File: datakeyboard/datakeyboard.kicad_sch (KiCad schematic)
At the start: 48 parts, among them Q1 NX2301P, Q2 NX2301P, Q3 NX2301P, Q4 NX2301P, Q5 NX2301P, SW1 SW_Push, SW2 SW_Push, SW3 SW_Push, SW4 SW_Push, SW5 SW_Push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

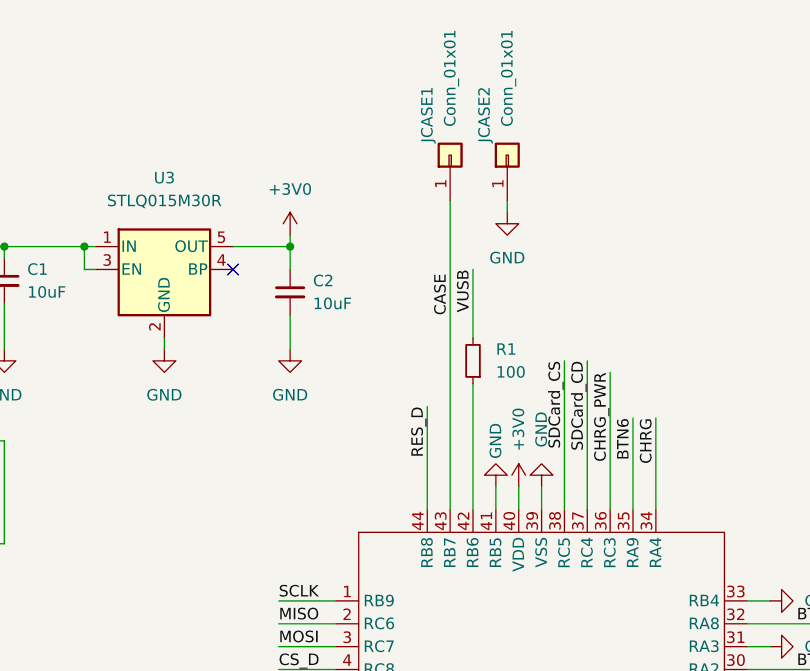
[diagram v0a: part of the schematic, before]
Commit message: Reduce current to increase battery life
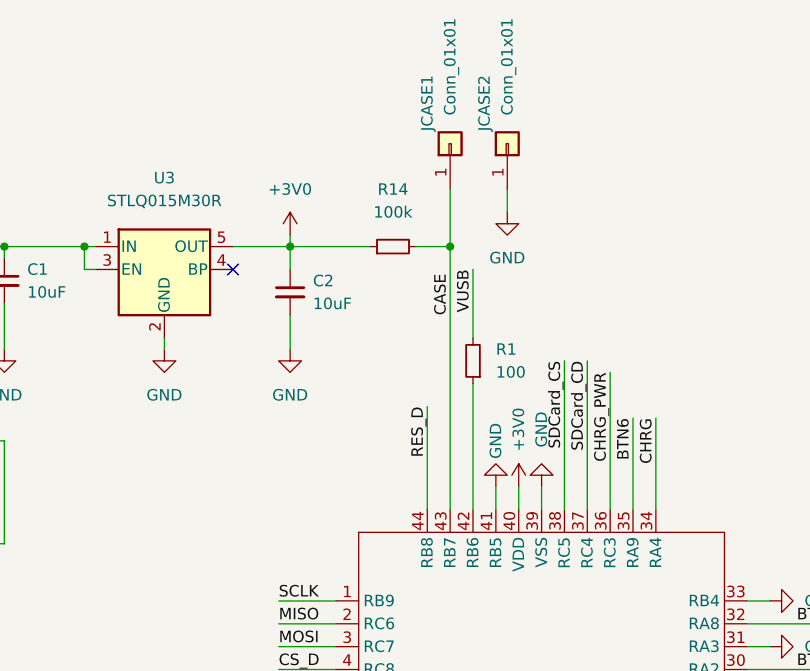
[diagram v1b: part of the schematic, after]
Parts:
- added R14: 100k, Resistor_SMD:R_0805_2012Metric_Pad1.20x1.40mm_HandSolder, symbol Device:R_Small
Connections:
- net +3V0: now also R14.1
- net CASE: now also R14.2
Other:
- moved on the sheet: JCASE1, JCASE2
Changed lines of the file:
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@@
   (junction (at 222.25 107.95) (diameter 0) (color 0 0 0 0)
+  )
+  (junction (at 144.78 38.1) (diameter 0) (color 0 0 0 0)
   )
   (junction (at 48.26 80.01) (diameter 0) (color 0 0 0 0)
@@
     (stroke (width 0) (type default) (color 0 0 0 0))
   )
+  (wire (pts (xy 140.97 38.1) (xy 144.78 38.1))
+    (stroke (width 0) (type default) (color 0 0 0 0))
+  )
   (wire (pts (xy 217.17 53.34) (xy 227.33 53.34))
     (stroke (width 0) (type default) (color 0 0 0 0))
@@
     (stroke (width 0) (type default) (color 0 0 0 0))
   )
+  (wire (pts (xy 127 38.1) (xy 135.89 38.1))
+    (stroke (width 0) (type default) (color 0 0 0 0))
+  )
   (wire (pts (xy 248.92 154.94) (xy 252.73 154.94))
     (stroke (width 0) (type default) (color 0 0 0 0))
@@
     (stroke (width 0) (type default) (color 0 0 0 0))
   )
-  (wire (pts (xy 144.78 33.02) (xy 144.78 67.31))
+  (wire (pts (xy 144.78 31.75) (xy 144.78 38.1))
     (stroke (width 0) (type default) (color 0 0 0 0))
   )
@@
     (stroke (width 0) (type default) (color 0 0 0 0))
   )
+  (wire (pts (xy 144.78 38.1) (xy 144.78 67.31))
+    (stroke (width 0) (type default) (color 0 0 0 0))
+  )
   (wire (pts (xy 270.51 60.96) (xy 271.78 60.96))
     (stroke (width 0) (type default) (color 0 0 0 0))
@@
     (stroke (width 0) (type default) (color 0 0 0 0))
   )
-  (wire (pts (xy 151.13 33.02) (xy 151.13 34.29))
+  (wire (pts (xy 151.13 31.75) (xy 151.13 34.29))
     (stroke (width 0) (type default) (color 0 0 0 0))
   )
@@
     (pin "2")
   )
-  (symbol (lib_id "Connector_Generic:Conn_01x01") (at 151.13 27.94 90) (unit 1)
+  (symbol (lib_id "Connector_Generic:Conn_01x01") (at 151.13 26.67 90) (unit 1)
     (in_bom yes) (on_board yes)
-    (property "Reference" "JCASE2" (id 0) (at 148.59 20.32 0)
+    (property "Reference" "JCASE2" (id 0) (at 148.59 19.05 0)
       (effects (font (size 1.27 1.27)) (justify right))
     )
-    (property "Value" "Conn_01x01" (id 1) (at 151.13 13.97 0)
+    (property "Value" "Conn_01x01" (id 1) (at 151.13 12.7 0)
       (effects (font (size 1.27 1.27)) (justify right))
     )
-    (property "Footprint" "TestPoint:TestPoint_Pad_2.0x2.0mm" (id 2) (at 151.13 27.94 0)
-      (effects (font (size 1.27 1.27)) hide)
-    )
-    (property "Datasheet" "~" (id 3) (at 151.13 27.94 0)
+    (property "Footprint" "TestPoint:TestPoint_Pad_2.0x2.0mm" (id 2) (at 151.13 26.67 0)
+      (effects (font (size 1.27 1.27)) hide)
+    )
+    (property "Datasheet" "~" (id 3) (at 151.13 26.67 0)
       (effects (font (size 1.27 1.27)) hide)
     )
@@
     (pin "2")
   )
-  (symbol (lib_id "Connector_Generic:Conn_01x01") (at 144.78 27.94 90) (unit 1)
+  (symbol (lib_id "Connector_Generic:Conn_01x01") (at 144.78 26.67 90) (unit 1)
     (in_bom yes) (on_board yes)
-    (property "Reference" "JCASE1" (id 0) (at 142.24 20.32 0)
+    (property "Reference" "JCASE1" (id 0) (at 142.24 19.05 0)
       (effects (font (size 1.27 1.27)) (justify right))
     )
-    (property "Value" "Conn_01x01" (id 1) (at 144.78 13.97 0)
+    (property "Value" "Conn_01x01" (id 1) (at 144.78 12.7 0)
       (effects (font (size 1.27 1.27)) (justify right))
     )
-    (property "Footprint" "TestPoint:TestPoint_Pad_2.0x2.0mm" (id 2) (at 144.78 27.94 0)
-      (effects (font (size 1.27 1.27)) hide)
-    )
-    (property "Datasheet" "~" (id 3) (at 144.78 27.94 0)
+    (property "Footprint" "TestPoint:TestPoint_Pad_2.0x2.0mm" (id 2) (at 144.78 26.67 0)
+      (effects (font (size 1.27 1.27)) hide)
+    )
+    (property "Datasheet" "~" (id 3) (at 144.78 26.67 0)
       (effects (font (size 1.27 1.27)) hide)
     )
@@
     (pin "1")
   )
+  (symbol (lib_id "Device:R_Small") (at 138.43 38.1 90) (unit 1)
+    (in_bom yes) (on_board yes) (fields_autoplaced)
+    (property "Reference" "R14" (id 0) (at 138.43 31.75 90))
+    (property "Value" "100k" (id 1) (at 138.43 34.29 90))
+    (property "Footprint" "Resistor_SMD:R_0805_2012Metric_Pad1.20x1.40mm_HandSolder" (id 2) (at 138.43 38.1 0)
+      (effects (font (size 1.27 1.27)) hide)
+    )
+    (property "Datasheet" "~" (id 3) (at 138.43 38.1 0)
+      (effects (font (size 1.27 1.27)) hide)
+    )
+    (pin "1")
+    (pin "2")
+  )
   (symbol (lib_id "Device:R_Small") (at 21.59 93.98 0) (unit 1)
     (in_bom yes) (on_board yes)
@@
       (reference "R13") (unit 1) (value "10k") (footprint "Resistor_SMD:R_0805_2012Metric_Pad1.20x1.40mm_HandSolder")
     )
+    (path "/c213b547-e739-4726-a3fd-495573c71a5a"
+      (reference "R14") (unit 1) (value "100k") (footprint "Resistor_SMD:R_0805_2012Metric_Pad1.20x1.40mm_HandSolder")
+    )
     (path "/064eada3-5eb6-40f4-8df6-485674836a12"
